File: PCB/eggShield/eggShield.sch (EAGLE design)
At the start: 35 parts, among them IC10 MCP601OT, IC3 LM339D, IC6 MCP601OT, IC7 MCP601OT

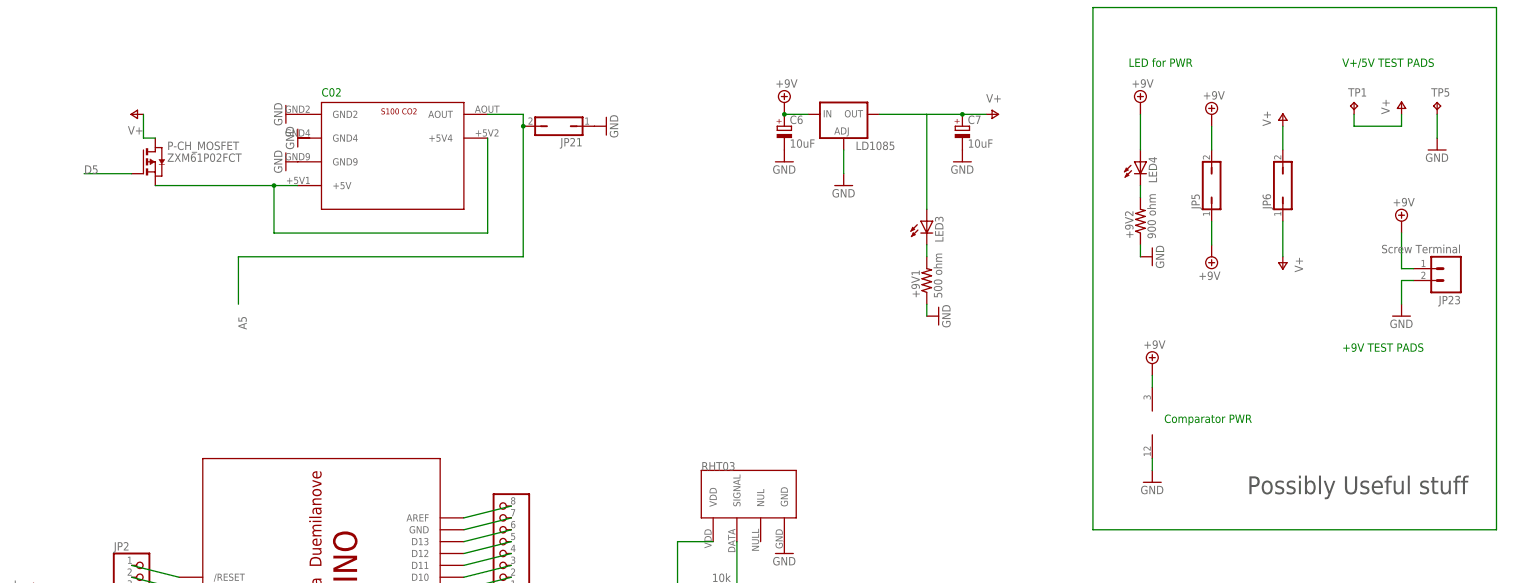
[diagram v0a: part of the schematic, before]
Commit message: added .brd, cleaned up
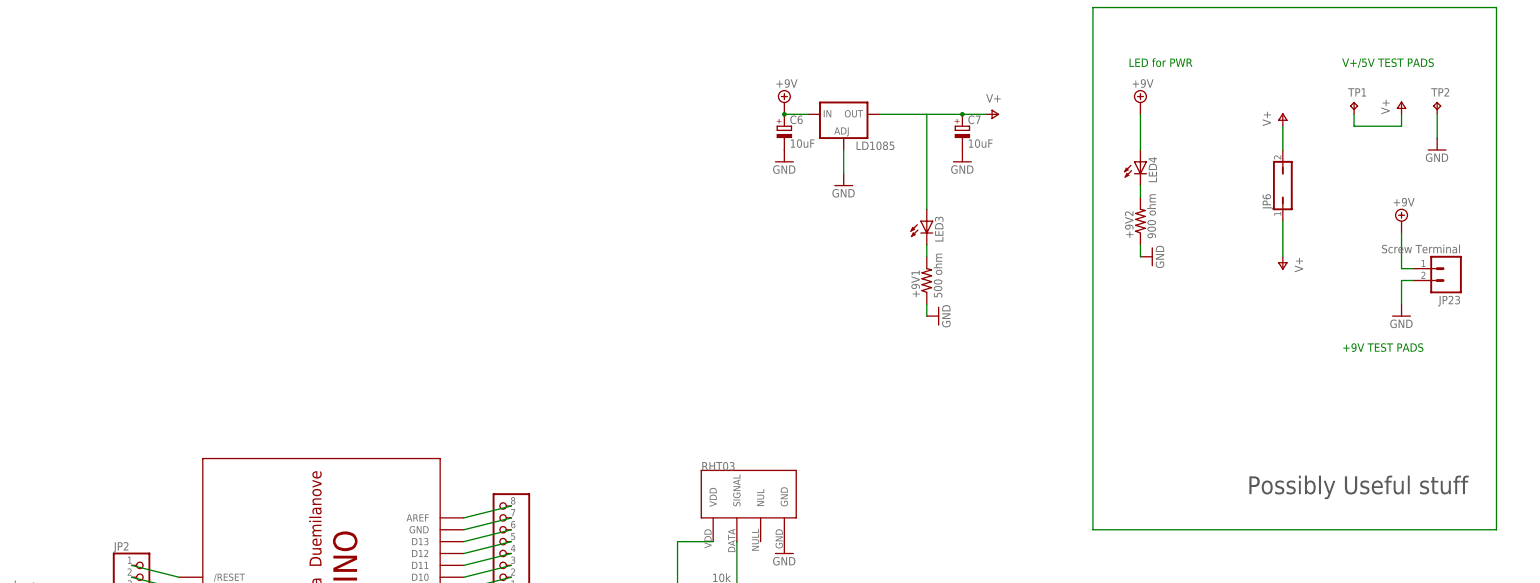
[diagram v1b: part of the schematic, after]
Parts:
- removed IC3: LM339D, linear:LM339D
- removed JP21, JP5: (no value), jumper:JP1Q
- removed P-CH_MOSFET: ZXM61P02FCT, zetex:PMOSSOT23
- removed U$6: S100CO2, ricardo:S100CO2
- renumbered TP5 to TP2
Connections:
- removed net A5: JP21.2, U$6.AOUT
- removed net D5: P-CH_MOSFET.G
- removed net N$49: P-CH_MOSFET.S, U$6.+5V, U$6.+5V4
- net +9V: no longer IC3P.V+, JP5.1, JP5.2
- net GND: no longer IC3P.GND, JP21.1, U$6.GND2, U$6.GND9
- net V+: no longer P-CH_MOSFET.D
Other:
- note removed: "C02"
- note removed: "Comparator PWR"
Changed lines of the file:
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@@
 <part name="P+1" library="supply1" deviceset="V+" device=""/>
 <part name="GND9" library="supply1" deviceset="GND" device=""/>
-<part name="IC3" library="linear" deviceset="LM339" device="D"/>
 <part name="SUPPLY6" library="supply2" deviceset="+9V" device=""/>
 <part name="LED3" library="SparkFun" deviceset="LED" device="3MM"/>
 <part name="GND22" library="supply1" deviceset="GND" device=""/>
 <part name="+9V1" library="rcl" deviceset="R-US_" device="R1206" value="500 ohm"/>
-<part name="U$6" library="ricardo" deviceset="S100CO2" device=""/>
-<part name="GND35" library="supply1" deviceset="GND" device=""/>
-<part name="GND36" library="supply1" deviceset="GND" device=""/>
-<part name="GND37" library="supply1" deviceset="GND" device=""/>
-<part name="P+13" library="supply1" deviceset="V+" device=""/>
 <part name="U$13" library="ricardo" deviceset="E2V" device=""/>
 <part name="GND46" library="supply1" deviceset="GND" device=""/>
@@
 <part name="GND48" library="supply1" deviceset="GND" device=""/>
 <part name="P+25" library="supply1" deviceset="V+" device=""/>
-<part name="JP5" library="jumper" deviceset="JP1Q" device=""/>
-<part name="SUPPLY12" library="supply2" deviceset="+9V" device=""/>
-<part name="SUPPLY13" library="supply2" deviceset="+9V" device=""/>
 <part name="JP6" library="jumper" deviceset="JP1Q" device=""/>
 <part name="P+33" library="supply1" deviceset="V+" device=""/>
@@
 <part name="+9V2" library="rcl" deviceset="R-US_" device="R1206" value="900 ohm"/>
 <part name="SUPPLY14" library="supply2" deviceset="+9V" device=""/>
-<part name="JP21" library="jumper" deviceset="JP1Q" device=""/>
-<part name="GND73" library="supply1" deviceset="GND" device=""/>
 <part name="NO2" library="ricardo" deviceset="E2V" device="" value="E2V NO2"/>
 <part name="GND25" library="supply1" deviceset="GND" device=""/>
@@
 <part name="TP1" library="testpad" deviceset="TP" device="PAD1-13Y"/>
 <part name="P+35" library="supply1" deviceset="V+" device=""/>
-<part name="P-CH_MOSFET" library="zetex" deviceset="PMOSSOT23" device="" value="ZXM61P02FCT"/>
 <part name="SUPPLY16" library="supply2" deviceset="+9V" device=""/>
 <part name="GND81" library="supply1" deviceset="GND" device=""/>
-<part name="TP5" library="testpad" deviceset="TP" device="PAD1-13Y">
+<part name="TP2" library="testpad" deviceset="TP" device="PAD1-13Y">
 <attribute name="TP_SIGNAL_NAME" value=""/>
 </part>
 <part name="GND82" library="supply1" deviceset="GND" device=""/>
 <part name="JP23" library="SparkFun" deviceset="M02" device="5MM" value="Screw Terminal"/>
-<part name="SUPPLY17" library="supply2" deviceset="+9V" device=""/>
-<part name="GND83" library="supply1" deviceset="GND" device=""/>
 <part name="IC6" library="linear" deviceset="MCP601" device="OT"/>
 <part name="P+37" library="supply1" deviceset="V+" device=""/>
@@
 <text x="419.1" y="274.32" size="1.778" layer="91">V+/5V TEST PADS</text>
 <text x="419.1" y="213.36" size="1.778" layer="91">+9V TEST PADS</text>
-<text x="381" y="198.12" size="1.778" layer="91">Comparator PWR</text>
 <text x="33.02" y="252.73" size="1.778" layer="91">NO2</text>
 <text x="34.036" y="168.402" size="1.778" layer="91">O3</text>
 <text x="33.02" y="212.09" size="1.778" layer="91">CO</text>
-<text x="200.66" y="267.97" size="1.778" layer="91">C02</text>
 <text x="398.78" y="182.88" size="3.81" layer="97">Possibly Useful stuff</text>
 </plain>
@@
 <instance part="GND22" gate="1" x="332.74" y="220.98" rot="R90"/>
 <instance part="+9V1" gate="G$1" x="330.2" y="228.6" rot="R90"/>
-<instance part="U$6" gate="G$1" x="213.36" y="256.54"/>
-<instance part="GND35" gate="1" x="193.04" y="264.16" rot="R270"/>
-<instance part="GND36" gate="1" x="195.58" y="259.08" rot="R270"/>
-<instance part="GND37" gate="1" x="193.04" y="254" rot="R270"/>
-<instance part="P+13" gate="1" x="160.02" y="264.16" rot="R90"/>
 <instance part="U$13" gate="G$1" x="48.26" y="200.66"/>
 <instance part="GND46" gate="1" x="25.4" y="205.74" rot="R270"/>
@@
 <instance part="GND48" gate="1" x="299.72" y="170.18"/>
 <instance part="P+25" gate="1" x="274.32" y="160.02" rot="R90"/>
-<instance part="JP5" gate="A" x="391.16" y="248.92"/>
-<instance part="SUPPLY12" gate="G$1" x="391.16" y="264.16"/>
-<instance part="SUPPLY13" gate="G$1" x="391.16" y="233.68" rot="R180"/>
 <instance part="JP6" gate="A" x="406.4" y="248.92"/>
 <instance part="P+33" gate="1" x="406.4" y="264.16"/>
@@
 <instance part="+9V2" gate="G$1" x="375.92" y="241.3" rot="R90"/>
 <instance part="SUPPLY14" gate="G$1" x="375.92" y="266.7"/>
-<instance part="JP21" gate="A" x="251.46" y="261.62" rot="R90"/>
-<instance part="GND73" gate="1" x="261.62" y="261.62" rot="R90"/>
 <instance part="NO2" gate="G$1" x="48.26" y="241.3"/>
 <instance part="GND25" gate="1" x="25.4" y="246.38" rot="R270"/>
@@
 <instance part="TP1" gate="G$1" x="421.64" y="266.7"/>
 <instance part="P+35" gate="1" x="431.8" y="266.7"/>
-<instance part="P-CH_MOSFET" gate="A" x="165.1" y="254"/>
 <instance part="SUPPLY16" gate="G$1" x="431.8" y="241.3"/>
 <instance part="GND81" gate="1" x="431.8" y="220.98"/>
-<instance part="TP5" gate="G$1" x="439.42" y="266.7"/>
+<instance part="TP2" gate="G$1" x="439.42" y="266.7"/>
 <instance part="GND82" gate="1" x="439.42" y="256.54"/>
 <instance part="JP23" gate="G$1" x="441.96" y="231.14" rot="R180"/>
-<instance part="IC3" gate="P" x="378.46" y="198.12"/>
-<instance part="SUPPLY17" gate="G$1" x="378.46" y="210.82"/>
-<instance part="GND83" gate="1" x="378.46" y="185.42"/>
 <instance part="IC6" gate="G$1" x="68.58" y="233.68"/>
 <instance part="P+37" gate="1" x="68.58" y="243.84"/>
@@
 </segment>
 <segment>
-<pinref part="U$6" gate="G$1" pin="GND9"/>
-<pinref part="GND37" gate="1" pin="GND"/>
-</segment>
-<segment>
 <pinref part="U$13" gate="G$1" pin="GND_HEATER"/>
 <pinref part="GND46" gate="1" pin="GND"/>
@@
 <pinref part="GND63" gate="1" pin="GND"/>
 <wire x1="375.92" y1="233.68" x2="375.92" y2="236.22" width="0.1524" layer="91"/>
-</segment>
-<segment>
-<pinref part="U$6" gate="G$1" pin="GND2"/>
-<pinref part="GND35" gate="1" pin="GND"/>
-</segment>
-<segment>
-<pinref part="JP21" gate="A" pin="1"/>
-<pinref part="GND73" gate="1" pin="GND"/>
 </segment>
 <segment>
@@
 <segment>
 <pinref part="GND82" gate="1" pin="GND"/>
-<pinref part="TP5" gate="G$1" pin="TP"/>
+<pinref part="TP2" gate="G$1" pin="TP"/>
 <wire x1="439.42" y1="264.16" x2="439.42" y2="259.08" width="0.1524" layer="91"/>
-</segment>
-<segment>
-<pinref part="IC3" gate="P" pin="GND"/>
-<pinref part="GND83" gate="1" pin="GND"/>
-<wire x1="378.46" y1="190.5" x2="378.46" y2="187.96" width="0.1524" layer="91"/>
 </segment>
 <segment>
@@
 </segment>
 <segment>
-<pinref part="P-CH_MOSFET" gate="A" pin="D"/>
-<pinref part="P+13" gate="1" pin="V+"/>
-<wire x1="165.1" y1="259.08" x2="162.56" y2="259.08" width="0.1524" layer="91"/>
-<wire x1="162.56" y1="259.08" x2="162.56" y2="264.16" width="0.1524" layer="91"/>
-</segment>
-<segment>
 <pinref part="IC6" gate="G$1" pin="V+"/>
 <pinref part="P+37" gate="1" pin="V+"/>
@@
 </segment>
 <segment>
-<pinref part="JP5" gate="A" pin="1"/>
-<pinref part="SUPPLY13" gate="G$1" pin="+9V"/>
-<wire x1="391.16" y1="241.3" x2="391.16" y2="236.22" width="0.1524" layer="91"/>
-</segment>
-<segment>
-<pinref part="JP5" gate="A" pin="2"/>
-<pinref part="SUPPLY12" gate="G$1" pin="+9V"/>
-<wire x1="391.16" y1="256.54" x2="391.16" y2="261.62" width="0.1524" layer="91"/>
-</segment>
-<segment>
 <pinref part="LED4" gate="G$1" pin="A"/>
 <wire x1="375.92" y1="264.16" x2="375.92" y2="256.54" width="0.1524" layer="91"/>
@@
 <pinref part="JP23" gate="G$1" pin="1"/>
 <wire x1="431.8" y1="231.14" x2="434.34" y2="231.14" width="0.1524" layer="91"/>
-</segment>
-<segment>
-<pinref part="SUPPLY17" gate="G$1" pin="+9V"/>
-<pinref part="IC3" gate="P" pin="V+"/>
-<wire x1="378.46" y1="208.28" x2="378.46" y2="205.74" width="0.1524" layer="91"/>
 </segment>
 <segment>
@@
 </segment>
 </net>
-<net name="N$49" class="0">
-<segment>
-<pinref part="P-CH_MOSFET" gate="A" pin="S"/>
-<pinref part="U$6" gate="G$1" pin="+5V"/>
-<wire x1="165.1" y1="248.92" x2="190.5" y2="248.92" width="0.1524" layer="91"/>
-<pinref part="U$6" gate="G$1" pin="+5V4"/>
-<wire x1="190.5" y1="248.92" x2="195.58" y2="248.92" width="0.1524" layer="91"/>
-<wire x1="236.22" y1="259.08" x2="236.22" y2="238.76" width="0.1524" layer="91"/>
-<wire x1="236.22" y1="238.76" x2="190.5" y2="238.76" width="0.1524" layer="91"/>
-<wire x1="190.5" y1="238.76" x2="190.5" y2="248.92" width="0.1524" layer="91"/>
-<junction x="190.5" y="248.92"/>
-</segment>
-</net>
-<net name="A5" class="0">
-<segment>
-<wire x1="243.84" y1="233.68" x2="243.84" y2="261.62" width="0.1524" layer="91"/>
-<pinref part="U$6" gate="G$1" pin="AOUT"/>
-<wire x1="243.84" y1="261.62" x2="243.84" y2="264.16" width="0.1524" layer="91"/>
-<wire x1="243.84" y1="264.16" x2="236.22" y2="264.16" width="0.1524" layer="91"/>
-<wire x1="243.84" y1="233.68" x2="182.88" y2="233.68" width="0.1524" layer="91"/>
-<wire x1="182.88" y1="233.68" x2="182.88" y2="223.52" width="0.1524" layer="91"/>
-<label x="182.88" y="220.98" size="1.778" layer="95" rot="R270"/>
-<pinref part="JP21" gate="A" pin="2"/>
-<junction x="243.84" y="261.62"/>
-</segment>
-</net>
-<net name="D5" class="0">
-<segment>
-<pinref part="P-CH_MOSFET" gate="A" pin="G"/>
-<wire x1="160.02" y1="251.46" x2="149.86" y2="251.46" width="0.1524" layer="91"/>
-<label x="149.86" y="251.46" size="1.778" layer="95"/>
-</segment>
-</net>

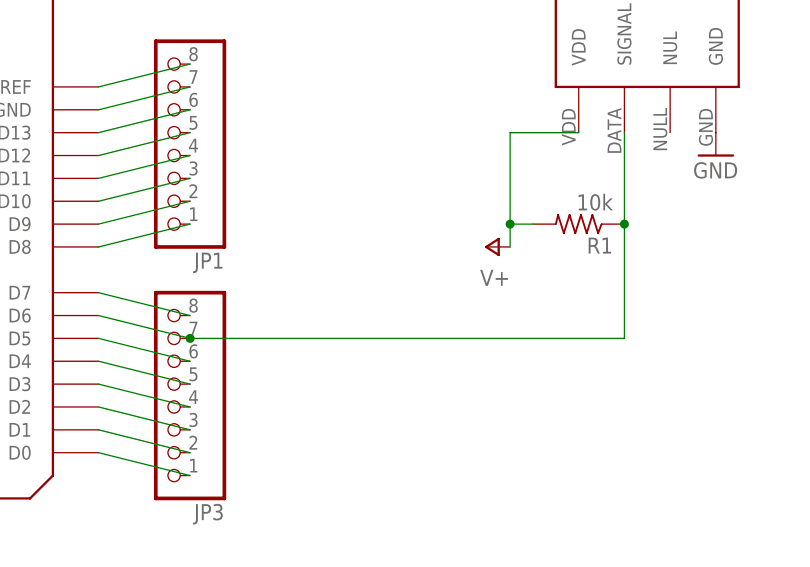
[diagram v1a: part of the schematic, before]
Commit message: fixed RHT pin
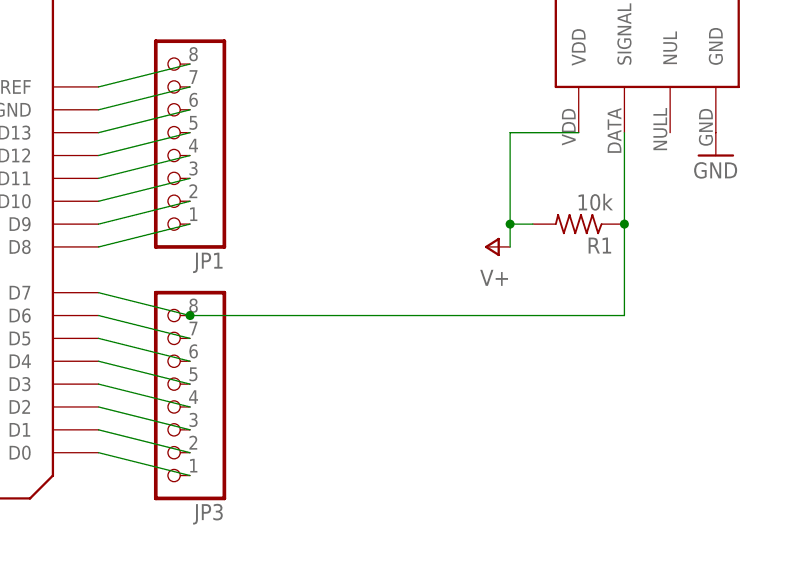
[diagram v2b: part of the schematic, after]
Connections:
- removed net N$21: JP3.8, U$2.D7
- new net N$5: JP3.7, U$2.D6
- net A3: now also JP3.8, U$2.D7; no longer JP3.7, U$2.D6
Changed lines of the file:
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@@
 <pinref part="U$14" gate="G$1" pin="SIGNAL"/>
 <wire x1="289.56" y1="172.72" x2="289.56" y2="162.56" width="0.1524" layer="91"/>
-<wire x1="289.56" y1="162.56" x2="289.56" y2="149.86" width="0.1524" layer="91"/>
+<wire x1="289.56" y1="162.56" x2="289.56" y2="152.4" width="0.1524" layer="91"/>
 <pinref part="R1" gate="G$1" pin="1"/>
 <junction x="289.56" y="162.56"/>
-<pinref part="U$2" gate="G$1" pin="D6"/>
-<pinref part="JP3" gate="G$1" pin="7"/>
-<wire x1="231.14" y1="152.4" x2="241.3" y2="149.86" width="0.1524" layer="91"/>
-<wire x1="241.3" y1="149.86" x2="289.56" y2="149.86" width="0.1524" layer="91"/>
-<junction x="241.3" y="149.86"/>
+<pinref part="U$2" gate="G$1" pin="D7"/>
+<pinref part="JP3" gate="G$1" pin="8"/>
+<wire x1="231.14" y1="154.94" x2="241.3" y2="152.4" width="0.1524" layer="91"/>
+<wire x1="289.56" y1="152.4" x2="241.3" y2="152.4" width="0.1524" layer="91"/>
+<junction x="241.3" y="152.4"/>
 </segment>
 </net>
@@
 </segment>
 </net>
-<net name="N$21" class="0">
-<segment>
-<pinref part="U$2" gate="G$1" pin="D7"/>
-<pinref part="JP3" gate="G$1" pin="8"/>
-<wire x1="231.14" y1="154.94" x2="241.3" y2="152.4" width="0.1524" layer="91"/>
-</segment>
-</net>
 <net name="N$22" class="0">
 <segment>
@@
 </segment>
 </net>
+<net name="N$5" class="0">
+<segment>
+<pinref part="JP3" gate="G$1" pin="7"/>
+<pinref part="U$2" gate="G$1" pin="D6"/>
+<wire x1="231.14" y1="152.4" x2="241.3" y2="149.86" width="0.1524" layer="91"/>
+</segment>
+</net>

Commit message: cleaned up a bit
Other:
- note added: "power"
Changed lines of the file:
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@@
 <text x="33.02" y="212.09" size="1.778" layer="91">CO</text>
 <text x="398.78" y="182.88" size="3.81" layer="97">Possibly Useful stuff</text>
+<text x="292.1" y="226.06" size="3.81" layer="97">power</text>
 </plain>
 <instances>
@@
 </segment>
 </net>
+<net name="N$6" class="0">
+<segment>
+<wire x1="284.48" y1="276.86" x2="284.48" y2="210.82" width="0.1524" layer="91"/>
+<wire x1="284.48" y1="210.82" x2="358.14" y2="210.82" width="0.1524" layer="91"/>
+<wire x1="358.14" y1="210.82" x2="358.14" y2="208.28" width="0.1524" layer="91"/>
+<wire x1="358.14" y1="210.82" x2="358.14" y2="276.86" width="0.1524" layer="91"/>
+<wire x1="358.14" y1="276.86" x2="284.48" y2="276.86" width="0.1524" layer="91"/>
+</segment>
+</net>

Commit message: updated sensor circuit, removed unneeded compnts
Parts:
- removed +9V1: 500 ohm, rcl:R-US_R1206
- removed IC10, IC6, IC7: MCP601OT, linear:MCP601OT
- removed JP6: (no value), jumper:JP1Q
- removed LED3: (no value), SparkFun:LED3MM
- removed TP1, TP2: TPPAD1-13Y, testpad:TPPAD1-13Y
- LD1085: value (none) -> V_REG_317SMD; device v-reg:LM138-TL -> SparkFun:V_REG_317SMD
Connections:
- removed net GND: +9V1.1, +9V2.1, C6.-, C7.-, IC10.V-, IC6.V-, IC7.V-, JP2.5, JP23.2, LD1085.ADJ, NO2.GND_HEATER, R21.2, R30.2, R5.2, TP2.TP, U$13.GND_HEATER, U$14.GND, U$2.GND1, U$9.GND_HEATER
- removed net N$19: +9V1.2, LED3.C
- removed net N$48: IC10.-IN, IC10.OUT, JP4.2, U$2.A1
- removed net N$52: IC6.-IN, IC6.OUT, JP4.1, U$2.A0
- removed net N$9: IC7.-IN, IC7.OUT, JP4.3, U$2.A2
- new net +5V: JP2.3, R1.2, U$14.VDD, U$2.5V
- new net 1.8: +9V2.1, C6.-, C7.-, JP2.5, JP23.2, LD1085.ADJ, NO2.GND_HEATER, R21.2, R30.2, R5.2, U$13.GND_HEATER, U$14.GND, U$2.GND1, U$9.GND_HEATER
- net N$47: now also JP4.2, U$2.A1; no longer IC10.+IN
- net N$50: now also JP4.1, U$2.A0; no longer IC6.+IN
- net N$55: now also JP4.3, U$2.A2; no longer IC7.+IN
- net V+: no longer IC10.V+, IC6.V+, IC7.V+, JP2.3, JP6.1, JP6.2, LED3.A, R1.2, TP1.TP, U$14.VDD, U$2.5V
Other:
- note added: "1.8v"
- moved on the sheet: C7
